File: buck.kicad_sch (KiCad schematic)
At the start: 10 parts

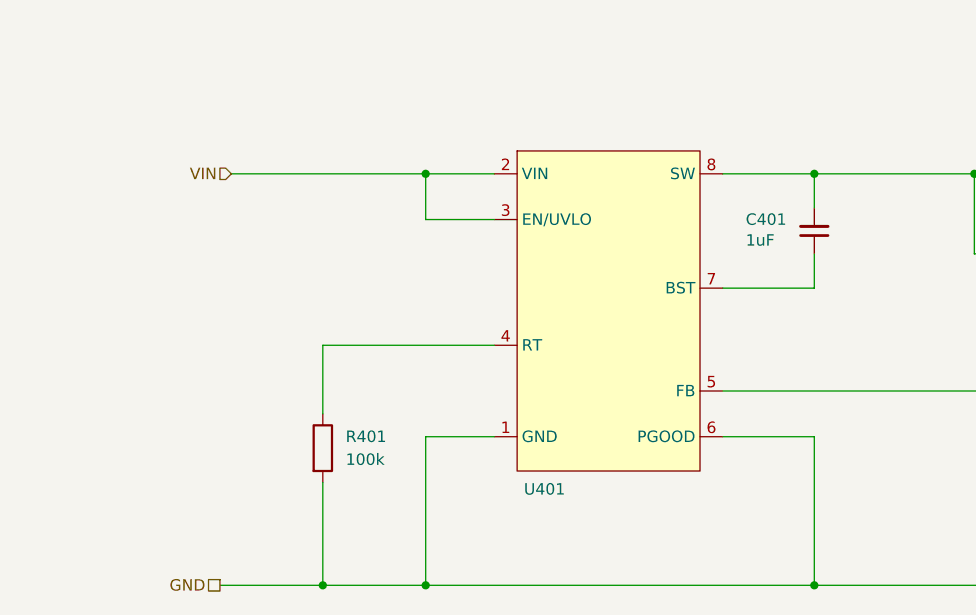
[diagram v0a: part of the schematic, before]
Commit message: added eeprom and isolation slots
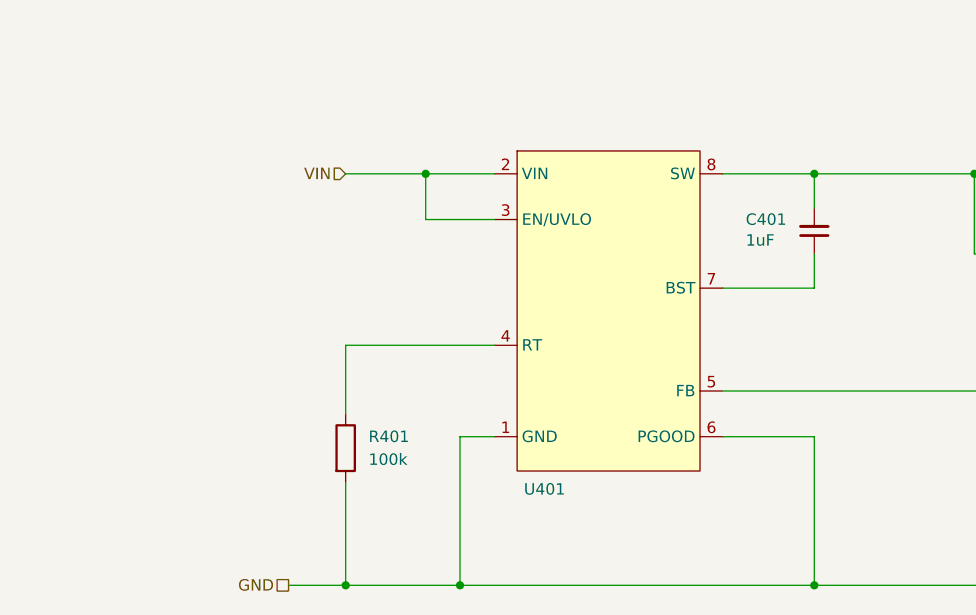
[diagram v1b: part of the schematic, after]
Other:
- moved on the sheet: R401

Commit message: feeder is routed
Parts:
- U401: footprint Package_SO:Texas_R-PDSO-G8_EP2.95x4.9mm_Mask2.4x3.1mm_ThermalVias -> Package_SO:SOIC-8-1EP_3.9x4.9mm_P1.27mm_EP2.29x3mm_ThermalVias
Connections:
- net GND: now also U401.9 (EP)
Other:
- note added: "VIN max: 120V"
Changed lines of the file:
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@@
 	(generator_version "10.0")
 	(paper "A4")
+	(text "VIN max: 120V"
+		(exclude_from_sim no)
+		(at 48.006 66.04 0)
+		(effects
+			(font
+				(size 1.27 1.27)
+			)
+		)
+	)
+	(junction
+		(at 67.31 119.38)
+		(diameter 0)
+		(color 0 0 0 0)
+	)
 	(junction
 		(at 38.1 119.38)
@@
 	(wire
 		(pts
+			(xy 67.31 119.38) (xy 90.17 119.38)
+		)
+		(stroke
+			(width 0.45)
+			(type default)
+		)
+	)
+	(wire
+		(pts
 			(xy 120.65 82.55) (xy 125.73 82.55)
 		)
@@
 	(wire
 		(pts
-			(xy 50.8 119.38) (xy 90.17 119.38)
+			(xy 50.8 119.38) (xy 67.31 119.38)
 		)
 		(stroke
@@
 		(stroke
 			(width 0)
+			(type default)
+		)
+	)
+	(wire
+		(pts
+			(xy 67.31 109.22) (xy 67.31 119.38)
+		)
+		(stroke
+			(width 0.45)
 			(type default)
 		)
@@
 		(length 2.54)
 		(shape round)
-		(at 166.37 125.73 0)
+		(at 19.05 125.73 0)
 		(effects
 			(font
@@
 		)
 		(property "Netclass" "PGND"
-			(at 166.9796 123.19 0)
+			(at 19.6596 123.19 0)
 			(show_name no)
 			(do_not_autoplace no)
@@
 		)
 		(property "Component Class" ""
-			(at 90.17 35.56 0)
+			(at -57.15 35.56 0)
 			(show_name no)
 			(do_not_autoplace no)
@@
 			)
 		)
-		(property "Description" ""
+		(property "Description" "Unpolarized capacitor, small symbol"
 			(at 125.73 90.17 0)
 			(hide yes)
@@
 			)
 		)
-		(property "Description" ""
+		(property "Description" "Resistor"
 			(at 147.32 107.95 0)
 			(hide yes)
@@
 			)
 		)
-		(property "Description" ""
+		(property "Description" "Resistor"
 			(at 38.1 104.14 0)
 			(hide yes)
@@
 			)
 		)
-		(property "Description" ""
+		(property "Description" "Unpolarized capacitor, small symbol"
 			(at 133.35 82.55 0)
 			(hide yes)
@@
 			)
 		)
-		(property "Description" ""
+		(property "Description" "Resistor"
 			(at 147.32 85.09 0)
 			(hide yes)
@@
 			)
 		)
-		(property "Description" ""
+		(property "Description" "Resistor"
 			(at 116.84 82.55 0)
 			(hide yes)
@@
 			)
 		)
-		(property "Description" ""
+		(property "Description" "Unpolarized capacitor, small symbol"
 			(at 90.17 80.01 0)
 			(hide yes)
@@
 			)
 		)
-		(property "Description" ""
+		(property "Description" "Unpolarized capacitor, small symbol"
 			(at 161.29 96.52 0)
 			(hide yes)
@@
 			)
 		)
-		(property "Footprint" "Package_SO:Texas_R-PDSO-G8_EP2.95x4.9mm_Mask2.4x3.1mm_ThermalVias"
+		(property "Footprint" "Package_SO:SOIC-8-1EP_3.9x4.9mm_P1.27mm_EP2.29x3mm_ThermalVias"
 			(at 67.31 83.82 0)
 			(hide yes)
@@
 			)
 		)
-		(property "Datasheet" ""
+		(property "Datasheet" "https://www.ti.com/lit/ds/symlink/lm5169.pdf"
 			(at 67.31 83.82 0)
 			(hide yes)
@@
 		)
 		(pin "8"
+		)
+		(pin "9"
 		)
 		(instances
@@
 			)
 		)
-		(property "Description" ""
+		(property "Description" "Inductor"
 			(at 124.46 73.66 0)
 			(hide yes)

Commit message: no erc errors
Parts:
- U401: footprint Package_SO:SOIC-8-1EP_3.9x4.9mm_P1.27mm_EP2.29x3mm_ThermalVias -> Package_SO:Texas_R-PDSO-G8_EP2.95x4.9mm_Mask2.4x3.1mm_ThermalVias
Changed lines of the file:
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@@
+	)
+	(junction
+		(at 165.1 73.66)
+		(diameter 0)
+		(color 0 0 0 0)
 	)
 	(junction
@@
 	(wire
 		(pts
-			(xy 161.29 73.66) (xy 170.18 73.66)
+			(xy 161.29 73.66) (xy 165.1 73.66)
 		)
 		(stroke
@@
 	(wire
 		(pts
+			(xy 165.1 71.12) (xy 165.1 73.66)
+		)
+		(stroke
+			(width 0)
+			(type default)
+		)
+	)
+	(wire
+		(pts
 			(xy 125.73 97.79) (xy 147.32 97.79)
 		)
@@
 	(wire
 		(pts
+			(xy 165.1 73.66) (xy 170.18 73.66)
+		)
+		(stroke
+			(width 0.4361)
+			(type default)
+		)
+	)
+	(wire
+		(pts
 			(xy 128.27 73.66) (xy 140.97 73.66)
 		)
@@
 			(width 0)
 			(type default)
-		)
-	)
-	(hierarchical_label "GND"
-		(shape passive)
-		(at 7.8585 3.3052 180)
-		(effects
-			(font
-				(size 1.27 1.27)
-			)
-			(justify right)
 		)
 	)
@@
 			)
 			(justify left)
-		)
-	)
-	(hierarchical_label "GND"
-		(shape passive)
-		(at 5.3185 0.7652 180)
-		(effects
-			(font
-				(size 1.27 1.27)
-			)
-			(justify right)
 		)
 	)
@@
 		(polyline
 			(pts
-				(xy 176.53 125.73) (xy 176.53 68.58) (xy 125.73 68.58) (xy 125.73 74.93) (xy 134.62 74.93) (xy 134.62 90.17)
+				(xy 176.53 125.73) (xy 176.53 64.77) (xy 125.73 64.77) (xy 125.73 74.93) (xy 134.62 74.93) (xy 134.62 90.17)
 				(xy 134.62 90.17) (xy 134.62 91.44) (xy 29.21 91.44) (xy 29.21 91.44) (xy 29.21 91.44) (xy 29.21 113.03)
 				(xy 16.51 113.03) (xy 16.51 125.73)
@@
 	)
 	(symbol
+		(lib_id "power:PWR_FLAG")
+		(at 165.1 71.12 0)
+		(unit 1)
+		(body_style 1)
+		(exclude_from_sim no)
+		(in_bom yes)
+		(on_board yes)
+		(in_pos_files yes)
+		(dnp no)
+		(property "Reference" "#FLG0401"
+			(at 165.1 69.215 0)
+			(hide yes)
+			(show_name no)
+			(do_not_autoplace no)
+			(effects
+				(font
+					(size 1.27 1.27)
+				)
+			)
+		)
+		(property "Value" "PWR_FLAG"
+			(at 165.1 67.31 0)
+			(show_name no)
+			(do_not_autoplace no)
+			(effects
+				(font
+					(size 1.27 1.27)
+				)
+			)
+		)
+		(property "Footprint" ""
+			(at 165.1 71.12 0)
+			(hide yes)
+			(show_name no)
+			(do_not_autoplace no)
+			(effects
+				(font
+					(size 1.27 1.27)
+				)
+			)
+		)
+		(property "Datasheet" ""
+			(at 165.1 71.12 0)
+			(hide yes)
+			(show_name no)
+			(do_not_autoplace no)
+			(effects
+				(font
+					(size 1.27 1.27)
+				)
+			)
+		)
+		(property "Description" "Special symbol for telling ERC where power comes from"
+			(at 165.1 71.12 0)
+			(hide yes)
+			(show_name no)
+			(do_not_autoplace no)
+			(effects
+				(font
+					(size 1.27 1.27)
+				)
+			)
+		)
+		(pin "1"
+		)
+		(instances
+			(project "Feeder"
+				(path "/8d0c1d66-35ef-4a53-a28f-436a11b54f42/224f8fc3-c1bb-4d94-8c49-0c22b3162449"
+					(reference "#FLG0401")
+					(unit 1)
+				)
+				(path "/8d0c1d66-35ef-4a53-a28f-436a11b54f42/2cdcb2ed-6c79-4c75-8125-df08284f401a"
+					(reference "#FLG0501")
+					(unit 1)
+				)
+			)
+		)
+	)
+	(symbol
 		(lib_id "Device:R")
 		(at 116.84 82.55 90)
@@
 			)
 		)
-		(property "Footprint" "Package_SO:SOIC-8-1EP_3.9x4.9mm_P1.27mm_EP2.29x3mm_ThermalVias"
+		(property "Footprint" "Package_SO:Texas_R-PDSO-G8_EP2.95x4.9mm_Mask2.4x3.1mm_ThermalVias"
 			(at 67.31 83.82 0)
 			(hide yes)

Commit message: v2 wip
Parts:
- added Q401: 2N7002, Package_TO_SOT_SMD:SOT-23, symbol Transistor_FET:2N7002
- added R405, R406: 499k, Footprints:R_0805_2012Metric, symbol Device:R
- added R407: 143k, Footprints:R_0805_2012Metric, symbol Device:R
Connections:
- net GND: now also Q401.2 (S), R407.2
- net VIN: now also R406.1; no longer U401.3 (EN/UVLO)
- new net: Q401.3 (D), R405.2, R407.1, U401.3 (EN/UVLO)
- new net: R405.1, R406.2
- new net ~{EN}: Q401.1 (G)
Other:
- note added: "EN/UVLO is active high, the signal needs to be at leasr 1.5V to work."
- note added: "If ~{EN} is high, then the buck is disabled"
- note added: "UVLO: Vin(ON) = 1.5 × (1 + Rᵤᵥ₁/Rᵤᵥ₂) Vin(OFF) = 1.4 × (1 + Rᵤᵥ₁/Rᵤᵥ₂)"
- note added: "Vin(ON) = 1.5 × (1 + 998k/Rᵤᵥ₂) Vin(OFF) = 1.4 × (1 + 998k/Rᵤᵥ₂)"
- moved on the sheet: C401, C402, C403, C404, L401, R401, R402, R403, R404, U401

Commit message: First layout complete - DRC not clear yet.
Signed-off-by: Jean Alinei <jean.alinei@owntech.org>
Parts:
- U401: footprint Package_SO:Texas_R-PDSO-G8_EP2.95x4.9mm_Mask2.4x3.1mm_ThermalVias -> Footprints:Texas_R-PDSO-G8_EP2.95x4.9mm_Mask2.4x3.1mm_ThermalVias
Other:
- moved on the sheet: C401, C402, C403, C404, L401, Q401, R401, R402, R403, R404, R405, R406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

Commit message: Slowly updating the feeder board
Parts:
- U401: value (none) -> LM5169PDDAR; LCSC (none) -> C5439798
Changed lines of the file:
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@@
 			)
 		)
-		(property "Value" ""
+		(property "Value" "LM5169PDDAR"
 			(at 162.56 91.44 0)
 			(show_name no)
@@
 			(at 162.56 91.44 0)
 			(hide yes)
+			(show_name no)
+			(do_not_autoplace no)
+			(effects
+				(font
+					(size 1.27 1.27)
+				)
+			)
+		)
+		(property "LCSC" "C5439798"
+			(at 162.56 91.44 0)
+			(hide yes)

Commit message: added propoer filter and rerouted filters + enhancements all arround the board. no drc errors except soic8 isolation
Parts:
- added C405, C406, C407, C408: 4.7u, Footprints:C_1210_3225Metric, symbol Device:C
- added L402: 10u, Inductor_SMD:L_Changjiang_FNR5040S, symbol Device:L
- added R408, R409: 2.2M, Resistor_SMD:R_0603_1608Metric, symbol Device:R_Small
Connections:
- net GND: now also C406.2, C408.2, R409.2
- net VIN: now also L402.1; no longer R406.1, U401.2 (VIN)
- new net: C405.2, C406.1, C407.2, C408.1, R408.2, R409.1
- new net VIN_{FILT}: C405.1, C407.1, L402.2, R406.1, R408.1, U401.2 (VIN)
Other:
- note added: "Input 12-110V @600mA max"
- note added: "LC FILTER: Ceq = @{((${/8d0c1d66-35ef-4a53-a28f-436a11b54f42/224f8fc3-c1bb-4d94-8c49-0c22b3162449/db1fe761-dd48-44fe-bf9d-b39cd18d39a7:Value}+${/8d0c1d66-35ef-4a53-a28f-436a11b54f42/224f8fc3-c1bb-4d94-8c49-0c22b3162449/983b22fd-f19c-4bc8-b83b-c61b05f953ac:Value})*(${/8d0c1d66-35ef-4a53-a28f-436a11b54f42/224f8fc3-c1bb-4d94-8c49-0c22b3162449/61097a98-3c14-424a-b0b7-b088217f3bd7:Value}+${/8d0c1d66-3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"
- note added: "f_SW = @{(12 * 2500) / ${/8d0c1d66-35ef-4a53-a28f-436a11b54f42/224f8fc3-c1bb-4d94-8c49-0c22b3162449/15dc1b4a-c674-4efa-8c19-09bbcad46af5:Value}*1000}kHz"
- moved on the sheet: R401

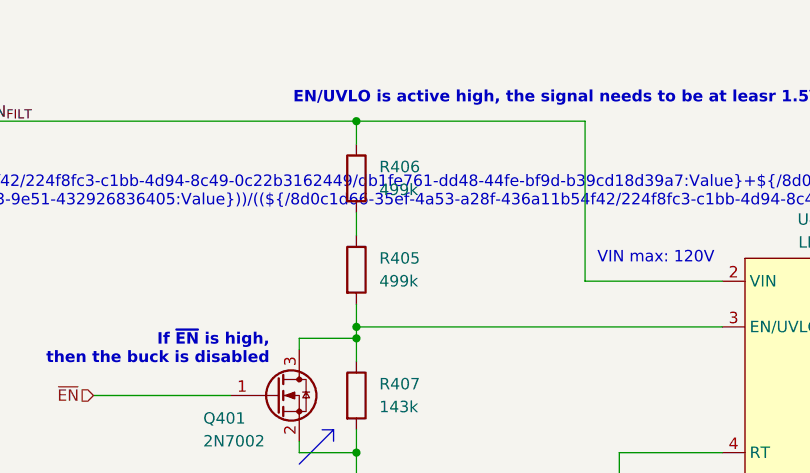
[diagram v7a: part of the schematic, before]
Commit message: Updated the DRC rules so it now checks correctly B4 and A6 IPC2221 rules
Signed-off-by: Jean Alinei <jean.alinei@owntech.org>
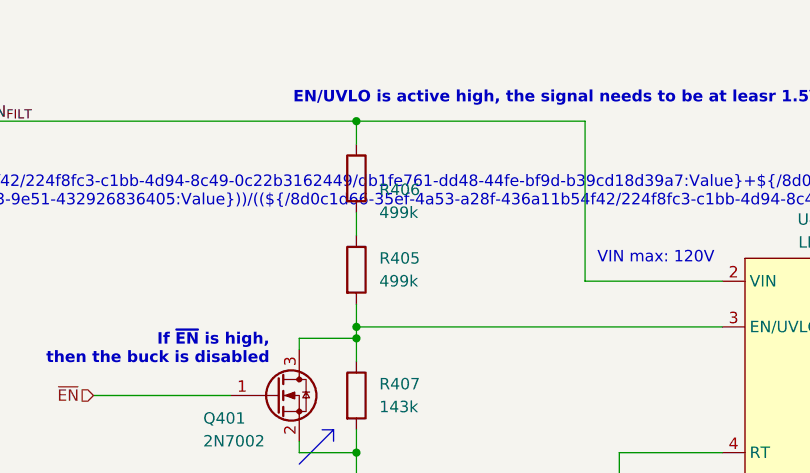
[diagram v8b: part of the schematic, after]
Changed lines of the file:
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@@
 		(polyline
 			(pts
-				(xy 17.78 77.47) (xy 68.58 77.47) (xy 68.58 74.93) (xy 129.54 74.93) (xy 129.54 82.55) (xy 157.48 82.55)
+				(xy 17.78 77.47) (xy 68.58 77.47) (xy 68.58 69.85) (xy 129.54 69.85) (xy 129.54 82.55) (xy 157.48 82.55)
 				(xy 157.48 57.15) (xy 17.78 57.15)
 			)
@@
 		(length 2.54)
 		(shape round)
-		(at 80.01 74.93 0)
+		(at 80.01 69.85 0)
 		(effects
 			(font
@@
 		)
 		(property "Netclass" "IBUS"
-			(at 79.4004 72.39 0)
+			(at 79.4004 67.31 0)
 			(show_name no)
 			(do_not_autoplace no)
@@
 		)
 		(property "Component Class" ""
-			(at 160.02 16.51 0)
+			(at 160.02 11.43 0)
 			(show_name no)
 			(do_not_autoplace no)
@@
 		(in_pos_files yes)
 		(dnp no)
-		(fields_autoplaced yes)
 		(property "Reference" "R406"
-			(at 111.76 68.5799 0)
+			(at 111.76 71.12 0)
 			(show_name no)
 			(do_not_autoplace no)
@@
 		)
 		(property "Value" "499k"
-			(at 111.76 71.1199 0)
+			(at 111.76 73.66 0)
 			(show_name no)
 			(do_not_autoplace no)
